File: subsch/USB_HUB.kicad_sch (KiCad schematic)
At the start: 7 parts

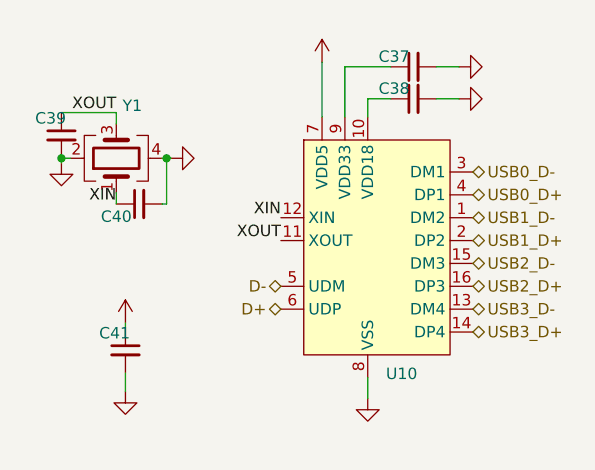
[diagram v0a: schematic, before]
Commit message: Add ESD protection
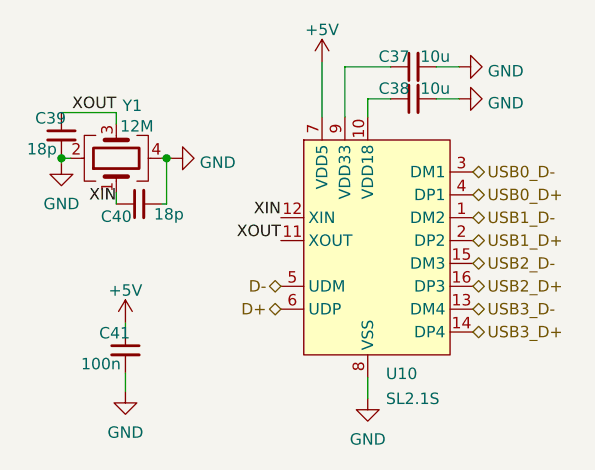
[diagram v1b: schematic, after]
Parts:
- C37, C38: value (none) -> 10u; footprint (none) -> Capacitor_SMD:C_0603_1608Metric
- C39, C40: value (none) -> 18p; footprint (none) -> Capacitor_SMD:C_0603_1608Metric
- C41: value (none) -> 100n; footprint (none) -> Capacitor_SMD:C_0603_1608Metric
- U10: value (none) -> SL2.1S; footprint (none) -> PcbLib:SL2.1S-SSOP-16
- Y1: value (none) -> 12M; footprint (none) -> Crystal:Crystal_SMD_3225-4Pin_3.2x2.5mm
